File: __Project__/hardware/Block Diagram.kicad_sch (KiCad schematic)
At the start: 0 parts

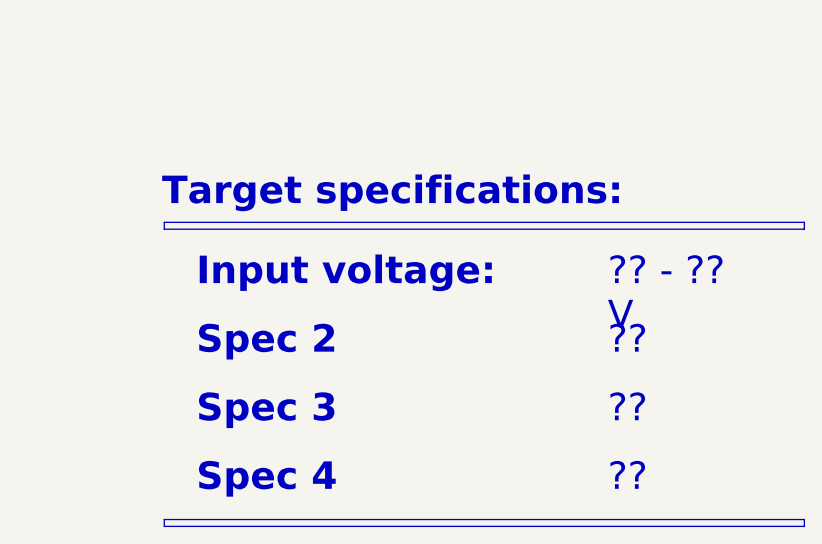
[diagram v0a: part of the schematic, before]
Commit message: Add Power and interface topology pages to KiBot template
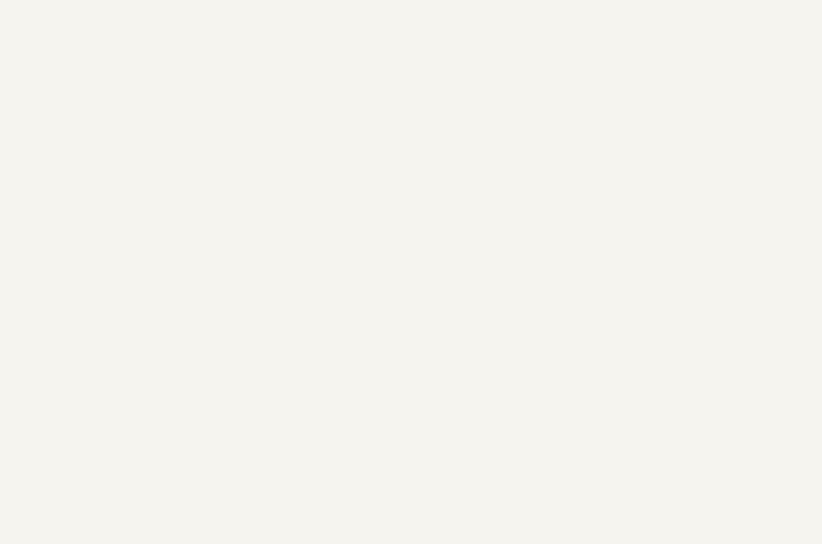
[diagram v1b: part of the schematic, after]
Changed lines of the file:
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@@
 		(company "${COMPANY}")
-	)
-	(rectangle
-		(start 328.422 234.95)
-		(end 399.542 235.712)
-		(stroke
-			(width 0)
-			(type default)
-			(color 0 0 0 1)
-		)
-		(fill
-			(type color)
-			(color 0 0 0 1)
-		)
-	)
-	(rectangle
-		(start 328.422 201.93)
-		(end 399.542 202.692)
-		(stroke
-			(width 0)
-			(type default)
-			(color 0 0 0 1)
-		)
-		(fill
-			(type color)
-			(color 0 0 0 1)
-		)
-	)
-	(text_box "Spec 4"
-		(exclude_from_sim no)
-		(at 329.692 226.06 0)
-		(size 44.45 7.62)
-		(margins 2.2859 2.2859 2.2859 2.2859)
-		(stroke
-			(width -0.0001)
-			(type default)
-		)
-		(fill
-			(type none)
-		)
-		(effects
-			(font
-				(face "Times New Roman")
-				(size 3.048 3.048)
-				(thickness 0.4572)
-				(bold yes)
-				(color 0 0 0 1)
-			)
-			(justify left top)
-		)
-	)
-	(text_box "?? - ?? V"
-		(exclude_from_sim no)
-		(at 375.412 203.2 0)
-		(size 24.13 7.62)
-		(margins 2.2859 2.2859 2.2859 2.2859)
-		(stroke
-			(width -0.0001)
-			(type default)
-		)
-		(fill
-			(type none)
-		)
-		(effects
-			(font
-				(face "Times New Roman")
-				(size 3.048 3.048)
-				(color 0 0 0 1)
-			)
-			(justify left top)
-		)
-	)
-	(text_box "??"
-		(exclude_from_sim no)
-		(at 375.412 226.06 0)
-		(size 24.13 7.62)
-		(margins 2.2859 2.2859 2.2859 2.2859)
-		(stroke
-			(width -0.0001)
-			(type default)
-		)
-		(fill
-			(type none)
-		)
-		(effects
-			(font
-				(face "Times New Roman")
-				(size 3.048 3.048)
-				(color 0 0 0 1)
-			)
-			(justify left top)
-		)
 	)
 	(text_box "[${#}] ${TITLE}"
@@
 		)
 	)
-	(text_box "??"
-		(exclude_from_sim no)
-		(at 375.412 210.82 0)
-		(size 24.13 7.62)
-		(margins 2.2859 2.2859 2.2859 2.2859)
-		(stroke
-			(width -0.0001)
-			(type default)
-		)
-		(fill
-			(type none)
-		)
-		(effects
-			(font
-				(face "Times New Roman")
-				(size 3.048 3.048)
-				(color 0 0 0 1)
-			)
-			(justify left top)
-		)
-	)
-	(text_box "Input voltage:"
-		(exclude_from_sim no)
-		(at 329.692 203.2 0)
-		(size 41.91 7.62)
-		(margins 2.2859 2.2859 2.2859 2.2859)
-		(stroke
-			(width -0.0001)
-			(type default)
-		)
-		(fill
-			(type none)
-		)
-		(effects
-			(font
-				(face "Times New Roman")
-				(size 3.048 3.048)
-				(thickness 0.4572)
-				(bold yes)
-				(color 0 0 0 1)
-			)
-			(justify left top)
-		)
-	)
-	(text_box "Target specifications:"
-		(exclude_from_sim no)
-		(at 325.882 194.31 0)
-		(size 73.66 7.62)
-		(margins 2.2859 2.2859 2.2859 2.2859)
-		(stroke
-			(width -0.0001)
-			(type default)
-		)
-		(fill
-			(type none)
-		)
-		(effects
-			(font
-				(face "Times New Roman")
-				(size 3.048 3.048)
-				(thickness 0.4572)
-				(bold yes)
-				(color 0 0 0 1)
-			)
-			(justify left top)
-		)
-	)
-	(text_box "Spec 3"
-		(exclude_from_sim no)
-		(at 329.692 218.44 0)
-		(size 41.91 7.62)
-		(margins 2.2859 2.2859 2.2859 2.2859)
-		(stroke
-			(width -0.0001)
-			(type default)
-		)
-		(fill
-			(type none)
-		)
-		(effects
-			(font
-				(face "Times New Roman")
-				(size 3.048 3.048)
-				(thickness 0.4572)
-				(bold yes)
-				(color 0 0 0 1)
-			)
-			(justify left top)
-		)
-	)
-	(text_box "??"
-		(exclude_from_sim no)
-		(at 375.412 218.44 0)
-		(size 24.13 7.62)
-		(margins 2.2859 2.2859 2.2859 2.2859)
-		(stroke
-			(width -0.0001)
-			(type default)
-		)
-		(fill
-			(type none)
-		)
-		(effects
-			(font
-				(face "Times New Roman")
-				(size 3.048 3.048)
-				(color 0 0 0 1)
-			)
-			(justify left top)
-		)
-	)
-	(text_box "Spec 2"
-		(exclude_from_sim no)
-		(at 329.692 210.82 0)
-		(size 43.18 7.62)
-		(margins 2.2859 2.2859 2.2859 2.2859)
-		(stroke
-			(width -0.0001)
-			(type default)
-		)
-		(fill
-			(type none)
-		)
-		(effects
-			(font
-				(face "Times New Roman")
-				(size 3.048 3.048)
-				(thickness 0.4572)
-				(bold yes)
-				(color 0 0 0 1)
-			)
-			(justify left top)
-		)
-	)

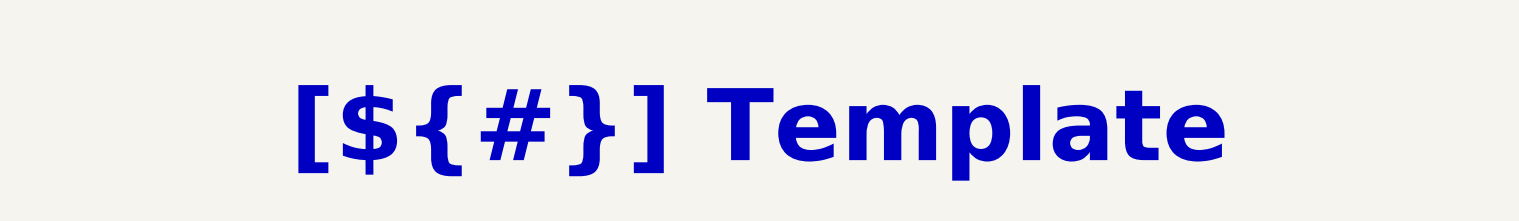
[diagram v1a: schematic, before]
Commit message: Fix JST footprints
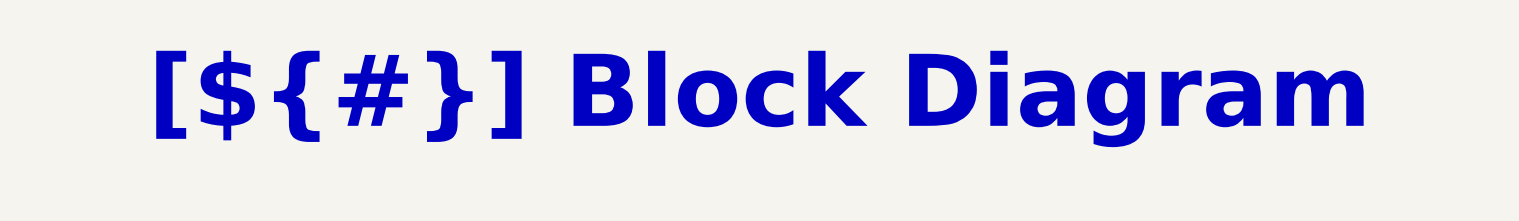
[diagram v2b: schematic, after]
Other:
- title: Template -> Block Diagram
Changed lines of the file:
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@@
 	(paper "A3")
 	(title_block
-		(title "Template")
+		(title "Block Diagram")
 		(date "2025-06-05")
 		(rev "${REVISION}")
@@
 	(text_box "[${#}] ${TITLE}"
 		(exclude_from_sim no)
-		(at 144.78 20.32 0)
-		(size 130.81 12.7)
+		(at 12.7 12.7 0)
+		(size 394.97 20.32)
 		(margins 5.9999 5.9999 5.9999 5.9999)
 		(stroke
